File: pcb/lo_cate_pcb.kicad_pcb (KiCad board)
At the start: 4 copper layers, 100 x 50 mm, 58 parts, among them J2 690-005-299-043, J3 Conn_01x09_Pin, SW1 MICRO_RESET, SW2 MICRO_ON, SW3 BUTTON1, SW4 BUTTON2, SW5 BUTTON3, U1 STM32F401RETx, U2 BMI323, U3 LED1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

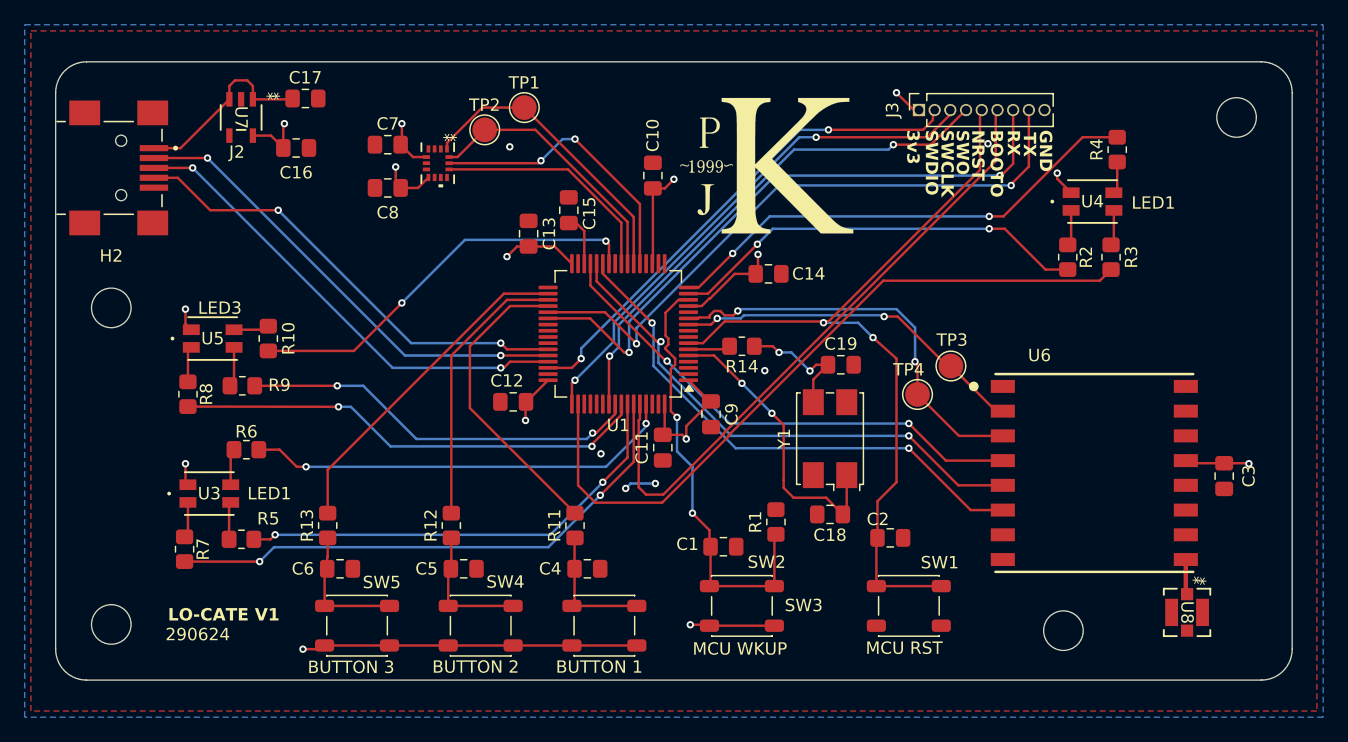
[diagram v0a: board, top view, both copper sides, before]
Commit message: Made changes the PCB to take it to version 2, bom just needs updating now
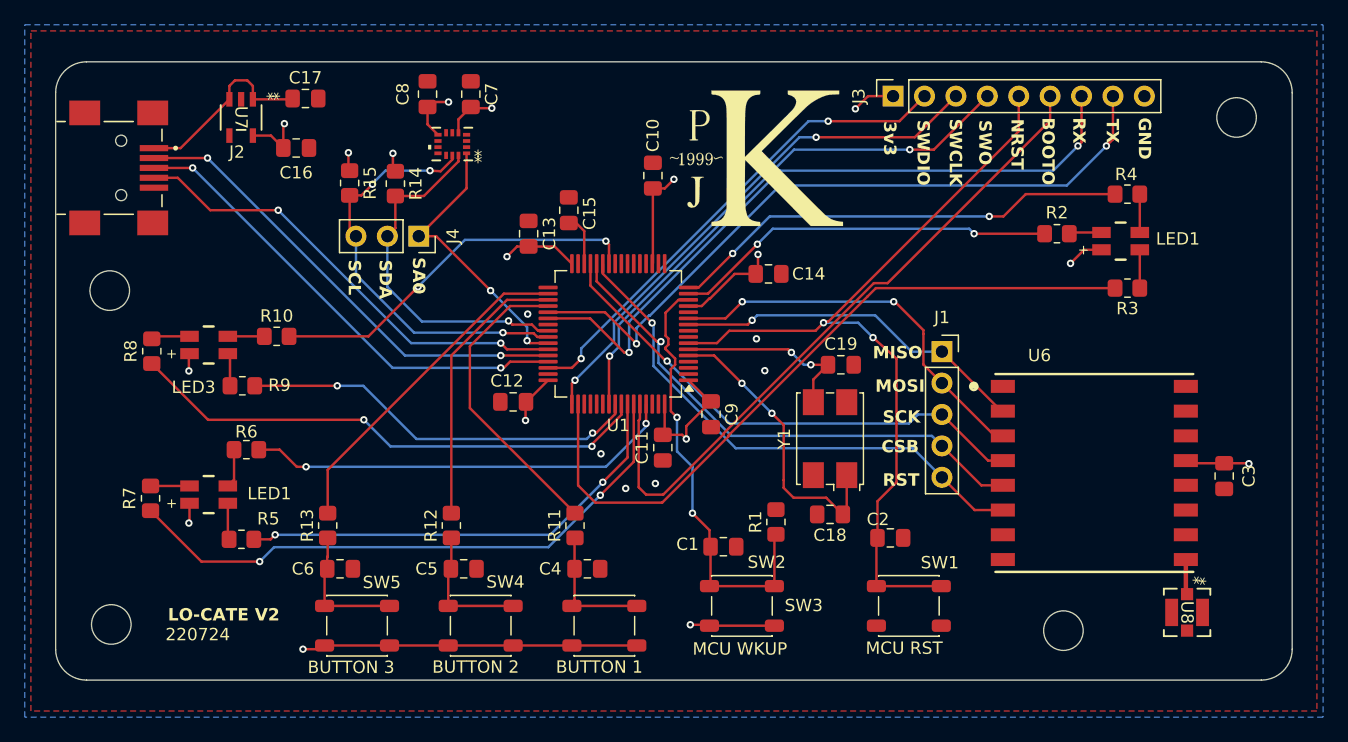
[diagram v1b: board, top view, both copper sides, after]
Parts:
- removed TP1: TP_IMU_MISO, TestPoint:TestPoint_Pad_D2.0mm
- removed TP2: TP_IMU_MOSI, TestPoint:TestPoint_Pad_D2.0mm
- removed TP3: TP_LORA_MISO, TestPoint:TestPoint_Pad_D2.0mm
- removed TP4: TP_LORA_MOSI, TestPoint:TestPoint_Pad_D2.0mm
- removed U3: LED1, footprints:150141M173100_WRE-M
- removed U4: LED2, footprints:150141M173100_WRE-M
- removed U5: LED3, footprints:150141M173100_WRE-M
- added D1: WL-SFTW_3528_PLCC4, footprints:WL-SFTW_3528_PLCC4, F.Cu at (109.9, 108.6)
- added D2: WL-SFTW_3528_PLCC4, footprints:WL-SFTW_3528_PLCC4, F.Cu at (183.7, 88.1)
- added D3: WL-SFTW_3528_PLCC4, footprints:WL-SFTW_3528_PLCC4, F.Cu at (109.9, 96.5)
- added J1: Conn_01x05_Pin, Connector_PinSocket_2.54mm:PinSocket_1x05_P2.54mm_Vertical, F.Cu at (169.2, 97.0)
- added J4: Conn_01x03_Pin, Connector_PinSocket_2.54mm:PinSocket_1x03_P2.54mm_Vertical, F.Cu at (126.9, 87.7)
- added R15: 60Ω, Resistor_SMD:R_0805_2012Metric_Pad1.20x1.40mm_HandSolder, F.Cu at (121.3, 83.4)
- C18, C19: value 10p -> 12p
- J3: footprint Connector_PinSocket_1.27mm:PinSocket_1x09_P1.27mm_Vertical -> Connector_PinSocket_2.54mm:PinSocket_1x09_P2.54mm_Vertical
- R14: value 30R -> 60Ω
- moved R14 31.0 mm to (125.0, 83.5), turned to -90 degrees
- moved C8 8.24 mm to (127.6, 76.2), turned to -90 degrees
- moved C7 7.86 mm to (131.1, 76.2), turned to -90 degrees
- moved R7 4.95 mm to (105.2, 108.9)
- moved R8 4.55 mm to (105.3, 97.0)
- moved R4 3.69 mm to (184.2, 84.3), turned to 180 degrees
- moved R3 2.83 mm to (184.2, 91.9), turned to 180 degrees
- moved J3 2.37 mm to (165.2, 76.4)
- moved R2 2.09 mm to (178.5, 87.5), turned to 0 degrees
- moved U2 1.95 mm to (129.6, 80.2), turned to 180 degrees
- moved H2 1.41 mm to (101.9, 92.1)
- moved G*** 1.02 mm to (154.2, 81.4)
- moved R10 0.70 mm to (115.4, 95.8), turned to 0 degrees
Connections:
- C19 pad 1: Net-(C19-Pad1) -> /OSC_OUT
- R14 pad 1: Net-(C19-Pad1) -> /3V3
- R14 pad 2: /OSC_OUT -> /IMU_SDA
- U1 pad 21: /IMU_SCK -> unconnected-(U1-PA5-Pad21)
- U1 pad 22: /IMU_MISO -> unconnected-(U1-PA6-Pad22)
- U1 pad 23: /IMU_MOSI -> unconnected-(U1-PA7-Pad23)
- U1 pad 24: /IMU_CSB -> unconnected-(U1-PC4-Pad24)
- U1 pad 40: unconnected-(U1-PC9-Pad40) -> /IMU_SDA
- U1 pad 41: unconnected-(U1-PA8-Pad41) -> /IMU_SCL
- U1 pad 42: unconnected-(U1-PA9-Pad42) -> /IMU_SA0
- U2 pad 1: /IMU_MISO -> /IMU_SA0
- U2 pad 12: /IMU_CSB -> unconnected-(U2-CSB-Pad12)
- U2 pad 13: /IMU_SCK -> /IMU_SCL
- U2 pad 14: /IMU_MOSI -> /IMU_SDA
- Y1 pad 3: Net-(C19-Pad1) -> /OSC_OUT
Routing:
- net /IMU_SCL: track 0.00 -> 34.3 mm, vias 0 -> 3
- net /IMU_SDA: track 0.00 -> 28.9 mm, vias 0 -> 1
- net /IMU_MISO: track 24.2 -> 0.00 mm
- net /IMU_SCK: track 23.2 -> 0.00 mm, vias 2 -> 0
- net /IMU_SA0: track 0.00 -> 23.1 mm, vias 0 -> 2
- net /IMU_MOSI: track 21.8 -> 0.00 mm
- net /IMU_CSB: track 19.0 -> 0.00 mm
- net /OSC_OUT: track 3.43 -> 15.3 mm, vias 0 -> 2
- net Net-(C19-Pad1): track 10.5 -> 0.00 mm, vias 2 -> 0
- net /UART_TX: track 51.6 -> 57.9 mm
- net /UART_RX: track 51.1 -> 56.5 mm
- net /3V3: track 97.8 -> 102.3 mm, vias 15 -> 17
- net /LED1_BLUE: track 44.3 -> 48.8 mm
- net /LED3_BLUE: track 38.6 -> 42.9 mm
- net /BOOTO: track 51.1 -> 54.8 mm
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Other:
- board text added: "220724"
- board text added: "CSB"
- board text added: "LO-CATE V2"
- board text added: "MISO"
- board text added: "MOSI"
- board text added: "RST"
- board text added: "SA0"
- board text added: "SCK"
- board text added: "SCL"
- board text added: "SDA"
- board text removed: "290624"
- board text removed: "LO-CATE V1"

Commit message: BOM Updated
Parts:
- R14, R15: value 60Ω -> 4.7K
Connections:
- U1 pad 21: unconnected-(U1-PA5-Pad21) -> /IMU_INT1
- U1 pad 22: unconnected-(U1-PA6-Pad22) -> /IMU_INT2
- U1 pad 51: unconnected-(U1-PC10-Pad51) -> /LORA_DIO0
- U1 pad 52: unconnected-(U1-PC11-Pad52) -> /LORA_DIO1
- U1 pad 53: unconnected-(U1-PC12-Pad53) -> /LORA_DIO2
- U2 pad 4: unconnected-(U2-INT1-Pad4) -> /IMU_INT1
- U2 pad 9: unconnected-(U2-INT2-Pad9) -> /IMU_INT2
- U6 pad 14: unconnected-(U6-DIO0-Pad14) -> /LORA_DIO0
- U6 pad 15: unconnected-(U6-DIO1-Pad15) -> /LORA_DIO1
- U6 pad 16: unconnected-(U6-DIO2-Pad16) -> /LORA_DIO2
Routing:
- net /LORA_DIO0: track 0.00 -> 61.7 mm, vias 0 -> 2
- net /LORA_DIO1: track 0.00 -> 61.0 mm, vias 0 -> 2
- net /LORA_DIO2: track 0.00 -> 59.5 mm, vias 0 -> 2
- net /IMU_INT2: track 0.00 -> 24.0 mm, vias 0 -> 2
- net /IMU_INT1: track 0.00 -> 19.0 mm
- net /LED2_RED: track 57.8 -> 59.4 mm
- net /LED1_GREEN: track 35.1 -> 35.0 mm, vias 2 -> 4
- net GND: vias 6 -> 5
